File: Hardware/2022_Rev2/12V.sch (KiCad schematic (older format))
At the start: 18 parts

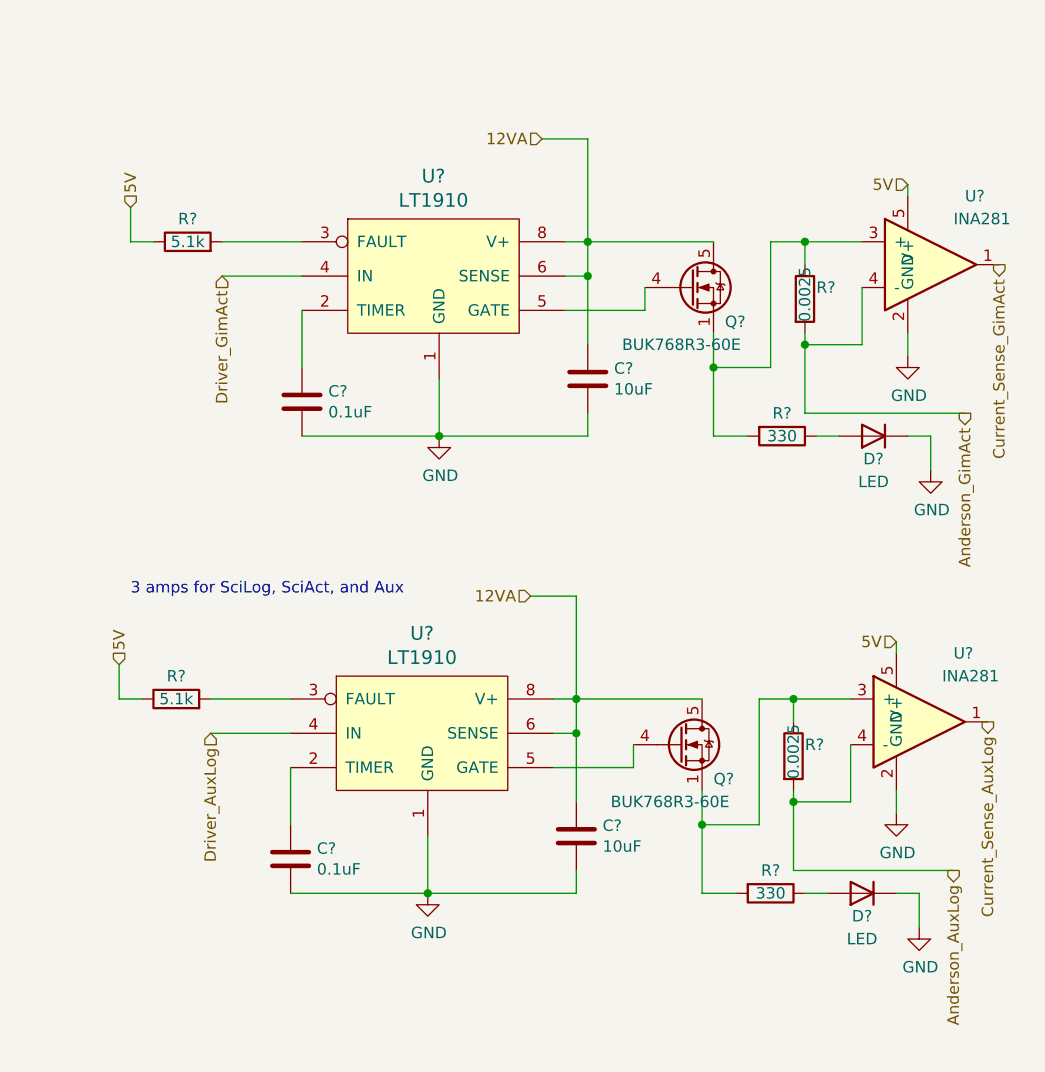
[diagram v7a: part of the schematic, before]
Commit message: assigning footprints pt.1
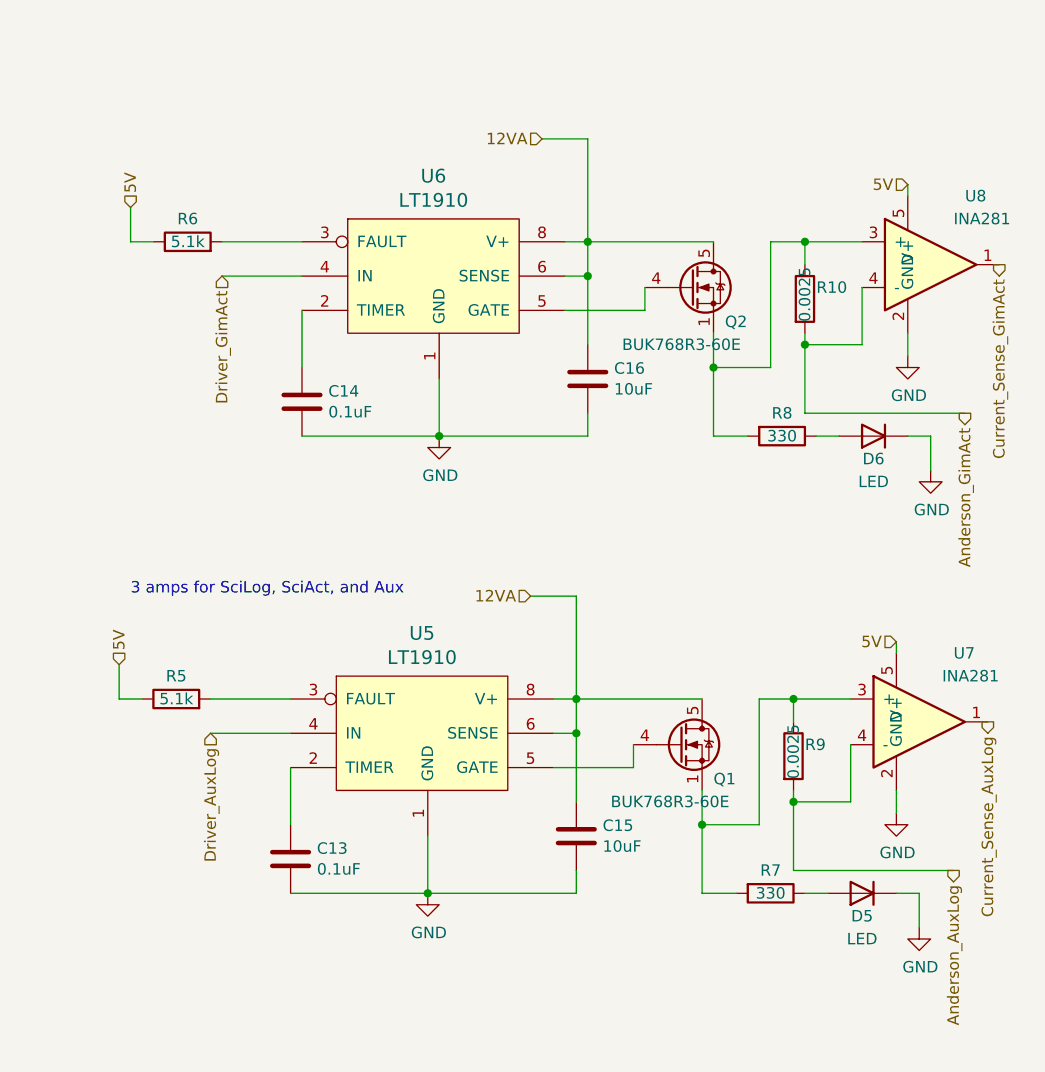
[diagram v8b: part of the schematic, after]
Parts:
- C13, C14, C15, C16: renamed from C?; footprint (none) -> Capacitor_SMD:C_0603_1608Metric_Pad1.08x0.95mm_HandSolder
- D5, D6: renamed from D?; footprint (none) -> Diode_SMD:D_0603_1608Metric_Pad1.05x0.95mm_HandSolder
- gave numbers to parts that had none: 12
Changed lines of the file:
@@
 P 7500 3000
 AR Path="/62118E70/621219B0/622FA100" Ref="R?"  Part="1"
-AR Path="/62118E70/622FA100" Ref="R?"  Part="1"
-F 0 "R?" V 7600 3000 50  0000 C CNN
+AR Path="/62118E70/622FA100" Ref="R6"  Part="1"
+F 0 "R6" V 7600 3000 50  0000 C CNN
 F 1 "5.1k" V 7500 3000 50  0000 C CNN
 F 2 "" V 7430 3000 50  0001 C CNN
@@
 P 8200 3400
 AR Path="/62118E70/621219B0/622FA106" Ref="U?"  Part="1"
-AR Path="/62118E70/622FA106" Ref="U?"  Part="1"
-F 0 "U?" H 8575 4087 60  0000 C CNN
+AR Path="/62118E70/622FA106" Ref="U6"  Part="1"
+F 0 "U6" H 8575 4087 60  0000 C CNN
 F 1 "LT1910" H 8575 3981 60  0000 C CNN
 F 2 "" H 8200 3400 60  0001 C CNN
@@
 P 8000 3700
 AR Path="/62118E70/621219B0/622FA10C" Ref="C?"  Part="1"
-AR Path="/62118E70/622FA10C" Ref="C?"  Part="1"
-F 0 "C?" H 8115 3746 50  0000 L CNN
+AR Path="/62118E70/622FA10C" Ref="C14"  Part="1"
+F 0 "C14" H 8115 3746 50  0000 L CNN
 F 1 "0.1uF" H 8115 3655 50  0000 L CNN
-F 2 "" H 8038 3550 50  0001 C CNN
+F 2 "Capacitor_SMD:C_0603_1608Metric_Pad1.08x0.95mm_HandSolder" H 8038 3550 50  0001 C CNN
 F 3 "~" H 8000 3700 50  0001 C CNN
 	1    8000 3700
@@
 P 8600 3850
 AR Path="/62118E70/621219B0/622FA112" Ref="#PWR?"  Part="1"
-AR Path="/62118E70/622FA112" Ref="#PWR?"  Part="1"
-F 0 "#PWR?" H 8600 3600 50  0001 C CNN
+AR Path="/62118E70/622FA112" Ref="#PWR0118"  Part="1"
+F 0 "#PWR0118" H 8600 3600 50  0001 C CNN
 F 1 "GND" H 8605 3677 50  0000 C CNN
 F 2 "" H 8600 3850 50  0001 C CNN
@@
 P 9250 3600
 AR Path="/62118E70/621219B0/622FA118" Ref="C?"  Part="1"
-AR Path="/62118E70/622FA118" Ref="C?"  Part="1"
-F 0 "C?" H 9365 3646 50  0000 L CNN
+AR Path="/62118E70/622FA118" Ref="C16"  Part="1"
+F 0 "C16" H 9365 3646 50  0000 L CNN
 F 1 "10uF" H 9365 3555 50  0000 L CNN
-F 2 "" H 9288 3450 50  0001 C CNN
+F 2 "Capacitor_SMD:C_0603_1608Metric_Pad1.08x0.95mm_HandSolder" H 9288 3450 50  0001 C CNN
 F 3 "~" H 9250 3600 50  0001 C CNN
 	1    9250 3600
@@
 P 9700 3200
 AR Path="/62118E70/621219B0/622FA11E" Ref="Q?"  Part="1"
-AR Path="/62118E70/622FA11E" Ref="Q?"  Part="1"
-F 0 "Q?" H 9850 3050 50  0000 L CNN
+AR Path="/62118E70/622FA11E" Ref="Q2"  Part="1"
+F 0 "Q2" H 9850 3050 50  0000 L CNN
 F 1 "BUK768R3-60E" H 9400 2950 50  0000 L CNN
 F 2 "Package_TO_SOT_SMD:LFPAK33" H 9900 3125 50  0001 L CIN
@@
 P 10100 3850
 AR Path="/62118E70/621219B0/622FA124" Ref="R?"  Part="1"
-AR Path="/62118E70/622FA124" Ref="R?"  Part="1"
-F 0 "R?" V 10000 3850 50  0000 C CNN
+AR Path="/62118E70/622FA124" Ref="R8"  Part="1"
+F 0 "R8" V 10000 3850 50  0000 C CNN
 F 1 "330" V 10100 3850 50  0000 C CNN
 F 2 "" V 10030 3850 50  0001 C CNN
@@
 P 10500 3850
 AR Path="/62118E70/621219B0/622FA12A" Ref="D?"  Part="1"
-AR Path="/62118E70/622FA12A" Ref="D?"  Part="1"
-F 0 "D?" H 10500 3950 50  0000 C CNN
+AR Path="/62118E70/622FA12A" Ref="D6"  Part="1"
+F 0 "D6" H 10500 3950 50  0000 C CNN
 F 1 "LED" H 10500 4050 50  0000 C CNN
-F 2 "" H 10500 3850 50  0001 C CNN
+F 2 "Diode_SMD:D_0603_1608Metric_Pad1.05x0.95mm_HandSolder" H 10500 3850 50  0001 C CNN
 F 3 "~" H 10500 3850 50  0001 C CNN
 	1    10500 3850
@@
 P 10650 3100
 AR Path="/62118E70/621219B0/622FA130" Ref="U?"  Part="1"
-AR Path="/62118E70/622FA130" Ref="U?"  Part="1"
-F 0 "U?" H 10900 3400 50  0000 L CNN
+AR Path="/62118E70/622FA130" Ref="U8"  Part="1"
+F 0 "U8" H 10900 3400 50  0000 L CNN
 F 1 "INA281" H 10850 3300 50  0000 L CNN
 F 2 "Package_TO_SOT_SMD:SOT-23-5" H 10900 3300 50  0001 C CNN
@@
 P 10750 4000
 AR Path="/62118E70/621219B0/622FA14C" Ref="#PWR?"  Part="1"
-AR Path="/62118E70/622FA14C" Ref="#PWR?"  Part="1"
-F 0 "#PWR?" H 10750 3750 50  0001 C CNN
+AR Path="/62118E70/622FA14C" Ref="#PWR0119"  Part="1"
+F 0 "#PWR0119" H 10750 3750 50  0001 C CNN
 F 1 "GND" H 10755 3827 50  0000 C CNN
 F 2 "" H 10750 4000 50  0001 C CNN
@@
 P 10200 3250
 AR Path="/62118E70/621219B0/622FA152" Ref="R?"  Part="1"
-AR Path="/62118E70/622FA152" Ref="R?"  Part="1"
-F 0 "R?" H 10250 3300 50  0000 L CNN
+AR Path="/62118E70/622FA152" Ref="R10"  Part="1"
+F 0 "R10" H 10250 3300 50  0000 L CNN
 F 1 "0.0025" V 10200 3150 50  0000 L CNN
 F 2 "" V 10130 3250 50  0001 C CNN
@@
 P 10650 3500
 AR Path="/62118E70/621219B0/622FA164" Ref="#PWR?"  Part="1"
-AR Path="/62118E70/622FA164" Ref="#PWR?"  Part="1"
-F 0 "#PWR?" H 10650 3250 50  0001 C CNN
+AR Path="/62118E70/622FA164" Ref="#PWR0120"  Part="1"
+F 0 "#PWR0120" H 10650 3250 50  0001 C CNN
 F 1 "GND" H 10655 3327 50  0000 C CNN
 F 2 "" H 10650 3500 50  0001 C CNN
@@
 AR Path="/62118E70/621219B0/624A08A6" Ref="R?"  Part="1"
 AR Path="/62118E70/622EFCD1/624A08A6" Ref="R?"  Part="1"
-AR Path="/62118E70/624A08A6" Ref="R?"  Part="1"
-F 0 "R?" V 7550 5000 50  0000 C CNN
+AR Path="/62118E70/624A08A6" Ref="R5"  Part="1"
+F 0 "R5" V 7550 5000 50  0000 C CNN
 F 1 "5.1k" V 7450 5000 50  0000 C CNN
 F 2 "" V 7380 5000 50  0001 C CNN
@@
 AR Path="/62118E70/621219B0/624A08AC" Ref="U?"  Part="1"
 AR Path="/62118E70/622EFCD1/624A08AC" Ref="U?"  Part="1"
-AR Path="/62118E70/624A08AC" Ref="U?"  Part="1"
-F 0 "U?" H 8525 6087 60  0000 C CNN
+AR Path="/62118E70/624A08AC" Ref="U5"  Part="1"
+F 0 "U5" H 8525 6087 60  0000 C CNN
 F 1 "LT1910" H 8525 5981 60  0000 C CNN
 F 2 "" H 8150 5400 60  0001 C CNN
@@
 AR Path="/62118E70/621219B0/624A08B2" Ref="C?"  Part="1"
 AR Path="/62118E70/622EFCD1/624A08B2" Ref="C?"  Part="1"
-AR Path="/62118E70/624A08B2" Ref="C?"  Part="1"
-F 0 "C?" H 8065 5746 50  0000 L CNN
+AR Path="/62118E70/624A08B2" Ref="C13"  Part="1"
+F 0 "C13" H 8065 5746 50  0000 L CNN
 F 1 "0.1uF" H 8065 5655 50  0000 L CNN
-F 2 "" H 7988 5550 50  0001 C CNN
+F 2 "Capacitor_SMD:C_0603_1608Metric_Pad1.08x0.95mm_HandSolder" H 7988 5550 50  0001 C CNN
 F 3 "~" H 7950 5700 50  0001 C CNN
 	1    7950 5700
@@
 AR Path="/62118E70/621219B0/624A08B8" Ref="#PWR?"  Part="1"
 AR Path="/62118E70/622EFCD1/624A08B8" Ref="#PWR?"  Part="1"
-AR Path="/62118E70/624A08B8" Ref="#PWR?"  Part="1"
-F 0 "#PWR?" H 8550 5600 50  0001 C CNN
+AR Path="/62118E70/624A08B8" Ref="#PWR0121"  Part="1"
+F 0 "#PWR0121" H 8550 5600 50  0001 C CNN
 F 1 "GND" H 8555 5677 50  0000 C CNN
 F 2 "" H 8550 5850 50  0001 C CNN
@@
 AR Path="/62118E70/621219B0/624A08BE" Ref="C?"  Part="1"
 AR Path="/62118E70/622EFCD1/624A08BE" Ref="C?"  Part="1"
-AR Path="/62118E70/624A08BE" Ref="C?"  Part="1"
-F 0 "C?" H 9315 5646 50  0000 L CNN
+AR Path="/62118E70/624A08BE" Ref="C15"  Part="1"
+F 0 "C15" H 9315 5646 50  0000 L CNN
 F 1 "10uF" H 9315 5555 50  0000 L CNN
-F 2 "" H 9238 5450 50  0001 C CNN
+F 2 "Capacitor_SMD:C_0603_1608Metric_Pad1.08x0.95mm_HandSolder" H 9238 5450 50  0001 C CNN
 F 3 "~" H 9200 5600 50  0001 C CNN
 	1    9200 5600
@@
 AR Path="/62118E70/621219B0/624A08C4" Ref="Q?"  Part="1"
 AR Path="/62118E70/622EFCD1/624A08C4" Ref="Q?"  Part="1"
-AR Path="/62118E70/624A08C4" Ref="Q?"  Part="1"
-F 0 "Q?" H 9800 5050 50  0000 L CNN
+AR Path="/62118E70/624A08C4" Ref="Q1"  Part="1"
+F 0 "Q1" H 9800 5050 50  0000 L CNN
 F 1 "BUK768R3-60E" H 9350 4950 50  0000 L CNN
 F 2 "Package_TO_SOT_SMD:LFPAK33" H 9850 5125 50  0001 L CIN
@@
 AR Path="/62118E70/621219B0/624A08CA" Ref="R?"  Part="1"
 AR Path="/62118E70/622EFCD1/624A08CA" Ref="R?"  Part="1"
-AR Path="/62118E70/624A08CA" Ref="R?"  Part="1"
-F 0 "R?" V 9950 5850 50  0000 C CNN
+AR Path="/62118E70/624A08CA" Ref="R7"  Part="1"
+F 0 "R7" V 9950 5850 50  0000 C CNN
 F 1 "330" V 10050 5850 50  0000 C CNN
 F 2 "" V 9980 5850 50  0001 C CNN
@@
 AR Path="/62118E70/621219B0/624A08D0" Ref="D?"  Part="1"
 AR Path="/62118E70/622EFCD1/624A08D0" Ref="D?"  Part="1"
-AR Path="/62118E70/624A08D0" Ref="D?"  Part="1"
-F 0 "D?" H 10450 5950 50  0000 C CNN
+AR Path="/62118E70/624A08D0" Ref="D5"  Part="1"
+F 0 "D5" H 10450 5950 50  0000 C CNN
 F 1 "LED" H 10450 6050 50  0000 C CNN
-F 2 "" H 10450 5850 50  0001 C CNN
+F 2 "Diode_SMD:D_0603_1608Metric_Pad1.05x0.95mm_HandSolder" H 10450 5850 50  0001 C CNN
 F 3 "~" H 10450 5850 50  0001 C CNN
 	1    10450 5850
@@
 AR Path="/62118E70/621219B0/624A08D6" Ref="U?"  Part="1"
 AR Path="/62118E70/622EFCD1/624A08D6" Ref="U?"  Part="1"
-AR Path="/62118E70/624A08D6" Ref="U?"  Part="1"
-F 0 "U?" H 10850 5400 50  0000 L CNN
+AR Path="/62118E70/624A08D6" Ref="U7"  Part="1"
+F 0 "U7" H 10850 5400 50  0000 L CNN
 F 1 "INA281" H 10800 5300 50  0000 L CNN
 F 2 "Package_TO_SOT_SMD:SOT-23-5" H 10850 5300 50  0001 C CNN
@@
 AR Path="/62118E70/621219B0/624A08F2" Ref="#PWR?"  Part="1"
 AR Path="/62118E70/622EFCD1/624A08F2" Ref="#PWR?"  Part="1"
-AR Path="/62118E70/624A08F2" Ref="#PWR?"  Part="1"
-F 0 "#PWR?" H 10700 5750 50  0001 C CNN
+AR Path="/62118E70/624A08F2" Ref="#PWR0122"  Part="1"
+F 0 "#PWR0122" H 10700 5750 50  0001 C CNN
 F 1 "GND" H 10705 5827 50  0000 C CNN
 F 2 "" H 10700 6000 50  0001 C CNN
@@
 AR Path="/62118E70/621219B0/624A08F8" Ref="R?"  Part="1"
 AR Path="/62118E70/622EFCD1/624A08F8" Ref="R?"  Part="1"
-AR Path="/62118E70/624A08F8" Ref="R?"  Part="1"
-F 0 "R?" H 10200 5300 50  0000 L CNN
+AR Path="/62118E70/624A08F8" Ref="R9"  Part="1"
+F 0 "R9" H 10200 5300 50  0000 L CNN
 F 1 "0.0025" V 10150 5150 50  0000 L CNN
 F 2 "" V 10080 5250 50  0001 C CNN
@@
 AR Path="/62118E70/621219B0/624A090A" Ref="#PWR?"  Part="1"
 AR Path="/62118E70/622EFCD1/624A090A" Ref="#PWR?"  Part="1"
-AR Path="/62118E70/624A090A" Ref="#PWR?"  Part="1"
-F 0 "#PWR?" H 10600 5250 50  0001 C CNN
+AR Path="/62118E70/624A090A" Ref="#PWR0123"  Part="1"
+F 0 "#PWR0123" H 10600 5250 50  0001 C CNN
 F 1 "GND" H 10605 5327 50  0000 C CNN
 F 2 "" H 10600 5500 50  0001 C CNN
